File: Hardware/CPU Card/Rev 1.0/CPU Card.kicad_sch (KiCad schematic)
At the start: 13 parts, among them J1 6502 Card Edge, J2 Conn_01x02, J3 Conn_02x05_Odd_Even, U1 65C02, X1 OCXO-14

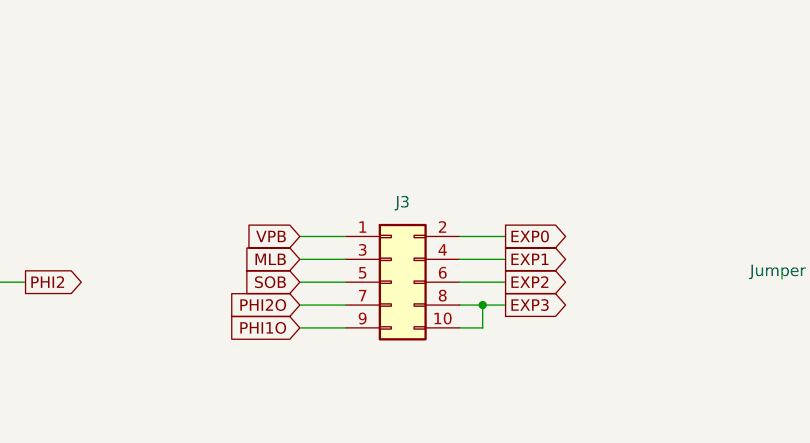
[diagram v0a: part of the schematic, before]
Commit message: CPU Card minor silkscreen fix
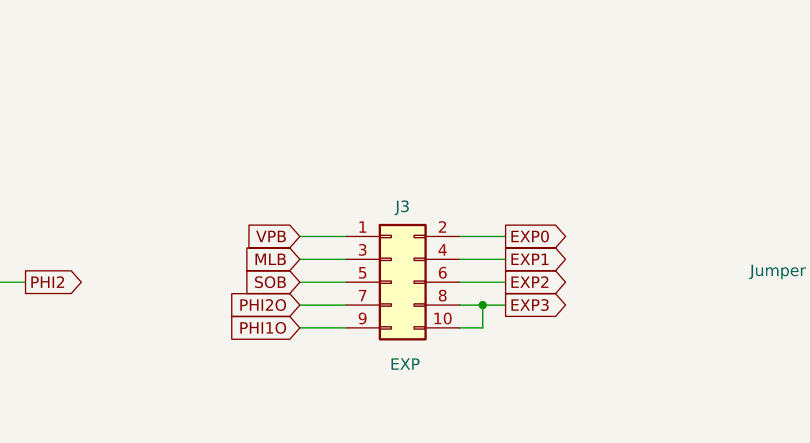
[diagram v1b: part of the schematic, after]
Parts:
- J3: value Conn_02x05_Odd_Even -> EXP
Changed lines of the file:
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@@
 		(on_board yes)
 		(dnp no)
-		(fields_autoplaced yes)
 		(property "Reference" "J3"
-			(at 105.41 135.89 0)
+			(at 105.41 136.398 0)
 			(effects
 				(font
@@
 			)
 		)
-		(property "Value" "Conn_02x05_Odd_Even"
-			(at 105.41 135.89 0)
+		(property "Value" "EXP"
+			(at 105.664 153.924 0)
 			(effects
 				(font
 					(size 1.27 1.27)
 				)
-				(hide yes)
 			)
 		)

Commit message: Remove oscillator from CPU cards
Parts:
- removed X1: OCXO-14, Oscillator:Oscillator_DIP-14, symbol Oscillator:OCXO-14
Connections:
- no-connect marks 1 -> 0
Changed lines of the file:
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@@
 		(color 0 0 0 0)
 	)
-	(no_connect
-		(at 39.37 144.78)
-	)
 	(wire
 		(pts
@@
 	(wire
 		(pts
-			(xy 52.07 134.62) (xy 52.07 137.16)
-		)
-		(stroke
-			(width 0)
-			(type default)
-		)
-	)
-	(wire
-		(pts
 			(xy 116.84 62.23) (xy 119.38 62.23)
 		)
@@
 	(wire
 		(pts
-			(xy 59.69 144.78) (xy 63.5 144.78)
-		)
-		(stroke
-			(width 0)
-			(type default)
-		)
-	)
-	(wire
-		(pts
 			(xy 52.07 95.25) (xy 54.61 95.25)
 		)
@@
 	(wire
 		(pts
-			(xy 52.07 152.4) (xy 52.07 154.94)
-		)
-		(stroke
-			(width 0)
-			(type default)
-		)
-	)
-	(wire
-		(pts
 			(xy 52.07 72.39) (xy 54.61 72.39)
 		)
@@
 		)
 	)
-	(global_label "VCC"
-		(shape input)
-		(at 52.07 134.62 90)
-		(fields_autoplaced yes)
-		(effects
-			(font
-				(size 1.27 1.27)
-			)
-			(justify left)
-		)
-		(property "Intersheetrefs" "${INTERSHEET_REFS}"
-			(at 52.07 128.6604 90)
-			(effects
-				(font
-					(size 1.27 1.27)
-				)
-				(justify left)
-				(hide yes)
-			)
-		)
-	)
 	(global_label "PHI1O"
 		(shape output)
@@
 		)
 	)
-	(global_label "PHI2"
-		(shape output)
-		(at 63.5 144.78 0)
-		(fields_autoplaced yes)
-		(effects
-			(font
-				(size 1.27 1.27)
-			)
-			(justify left)
-		)
-		(property "Intersheetrefs" "${INTERSHEET_REFS}"
-			(at 70.2458 144.78 0)
-			(effects
-				(font
-					(size 1.27 1.27)
-				)
-				(justify left)
-				(hide yes)
-			)
-		)
-	)
 	(global_label "SOB"
 		(shape input)
@@
 	)
 	(symbol
-		(lib_id "Oscillator:OCXO-14")
-		(at 52.07 144.78 0)
-		(unit 1)
-		(exclude_from_sim no)
-		(in_bom no)
-		(on_board yes)
-		(dnp no)
-		(property "Reference" "X1"
-			(at 43.434 137.414 0)
-			(effects
-				(font
-					(size 1.27 1.27)
-				)
-			)
-		)
-		(property "Value" "OCXO-14"
-			(at 63.5 141.0014 0)
-			(effects
-				(font
-					(size 1.27 1.27)
-				)
-				(hide yes)
-			)
-		)
-		(property "Footprint" "Oscillator:Oscillator_DIP-14"
-			(at 63.5 153.67 0)
-			(effects
-				(font
-					(size 1.27 1.27)
-				)
-				(hide yes)
-			)
-		)
-		(property "Datasheet" "http://www.petermann-technik.de/fileadmin/petermann/pdf/crystal-oscillators/OCXO-14_PETERMANN-TECHNIK.pdf"
-			(at 44.45 142.24 0)
-			(effects
-				(font
-					(size 1.27 1.27)
-				)
-				(hide yes)
-			)
-		)
-		(property "Description" "Voltage-Controlled Crystal Clock Oscillator, DIP14-style metal package"
-			(at 52.07 144.78 0)
-			(effects
-				(font
-					(size 1.27 1.27)
-				)
-				(hide yes)
-			)
-		)
-		(pin "14"
-		)
-		(pin "1"
-		)
-		(pin "7"
-		)
-		(pin "8"
-		)
-		(instances
-			(project "CPU Card"
-				(path "/b93a1794-fe4c-46dd-b3af-a8a2c2dc45ce"
-					(reference "X1")
-					(unit 1)
-				)
-			)
-		)
-	)
-	(symbol
 		(lib_id "Device:R")
 		(at 208.28 91.44 270)
@@
 					(unit 1)
 				)
-			)
-		)
-	)
-	(symbol
-		(lib_id "power:GND")
-		(at 52.07 154.94 0)
-		(unit 1)
-		(exclude_from_sim no)
-		(in_bom yes)
-		(on_board yes)
-		(dnp no)
-		(property "Reference" "#PWR04"
-			(at 52.07 161.29 0)
-			(effects
-				(font
-					(size 1.27 1.27)
-				)
-				(hide yes)
-			)
-		)
-		(property "Value" "GND"
-			(at 52.197 159.3342 0)
-			(effects
-				(font
-					(size 1.27 1.27)
-				)
-			)
-		)
-		(property "Footprint" ""
-			(at 52.07 154.94 0)
-			(effects
-				(font
-					(size 1.27 1.27)
-				)
-				(hide yes)
-			)
-		)
-		(property "Datasheet" ""
-			(at 52.07 154.94 0)
-			(effects
-				(font
-					(size 1.27 1.27)
-				)
-				(hide yes)
-			)
-		)
-		(property "Description" "Power symbol creates a global label with name \"GND\" , ground"
-			(at 52.07 154.94 0)
-			(effects
-				(font
-					(size 1.27 1.27)
-				)
-				(hide yes)
-			)
-		)
-		(pin "1"
-		)
-		(instances
-			(project "CPU Card"
-				(path "/b93a1794-fe4c-46dd-b3af-a8a2c2dc45ce"
-					(reference "#PWR04")
-					(unit 1)
-				)
